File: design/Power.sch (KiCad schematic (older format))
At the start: 50 parts, among them U2 DRV8302, U3 NCP1117ST33T3G

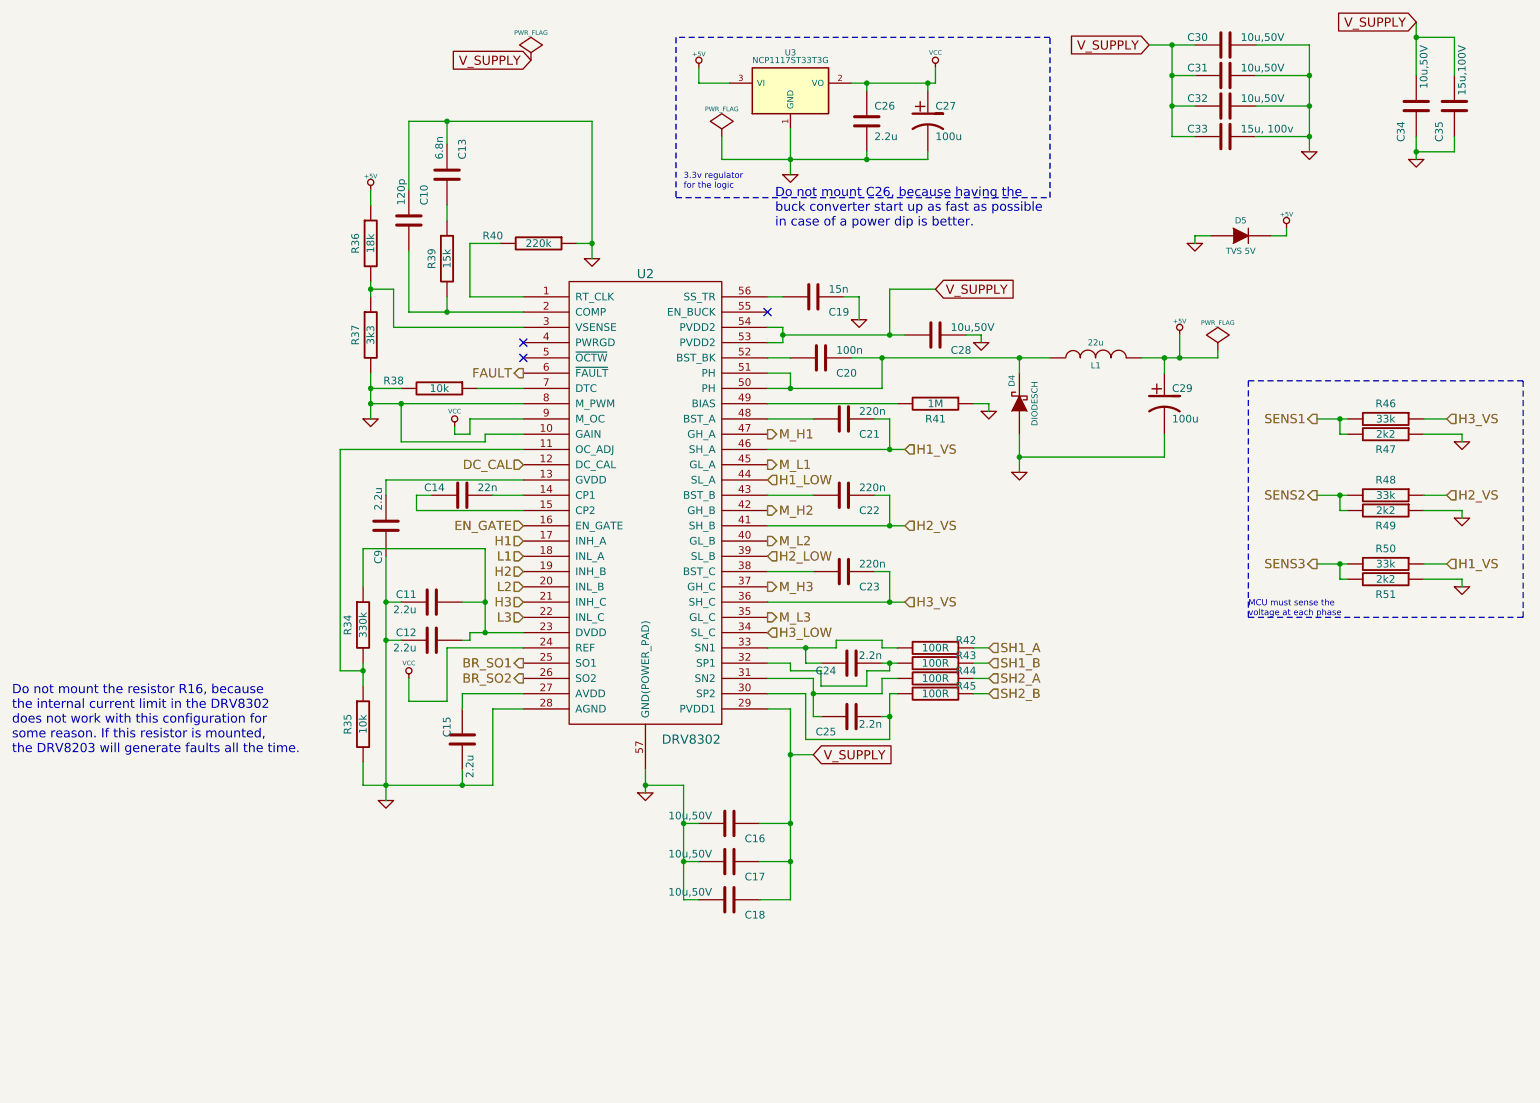
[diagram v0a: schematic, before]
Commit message: Add a voltage divider resistors for driver chip
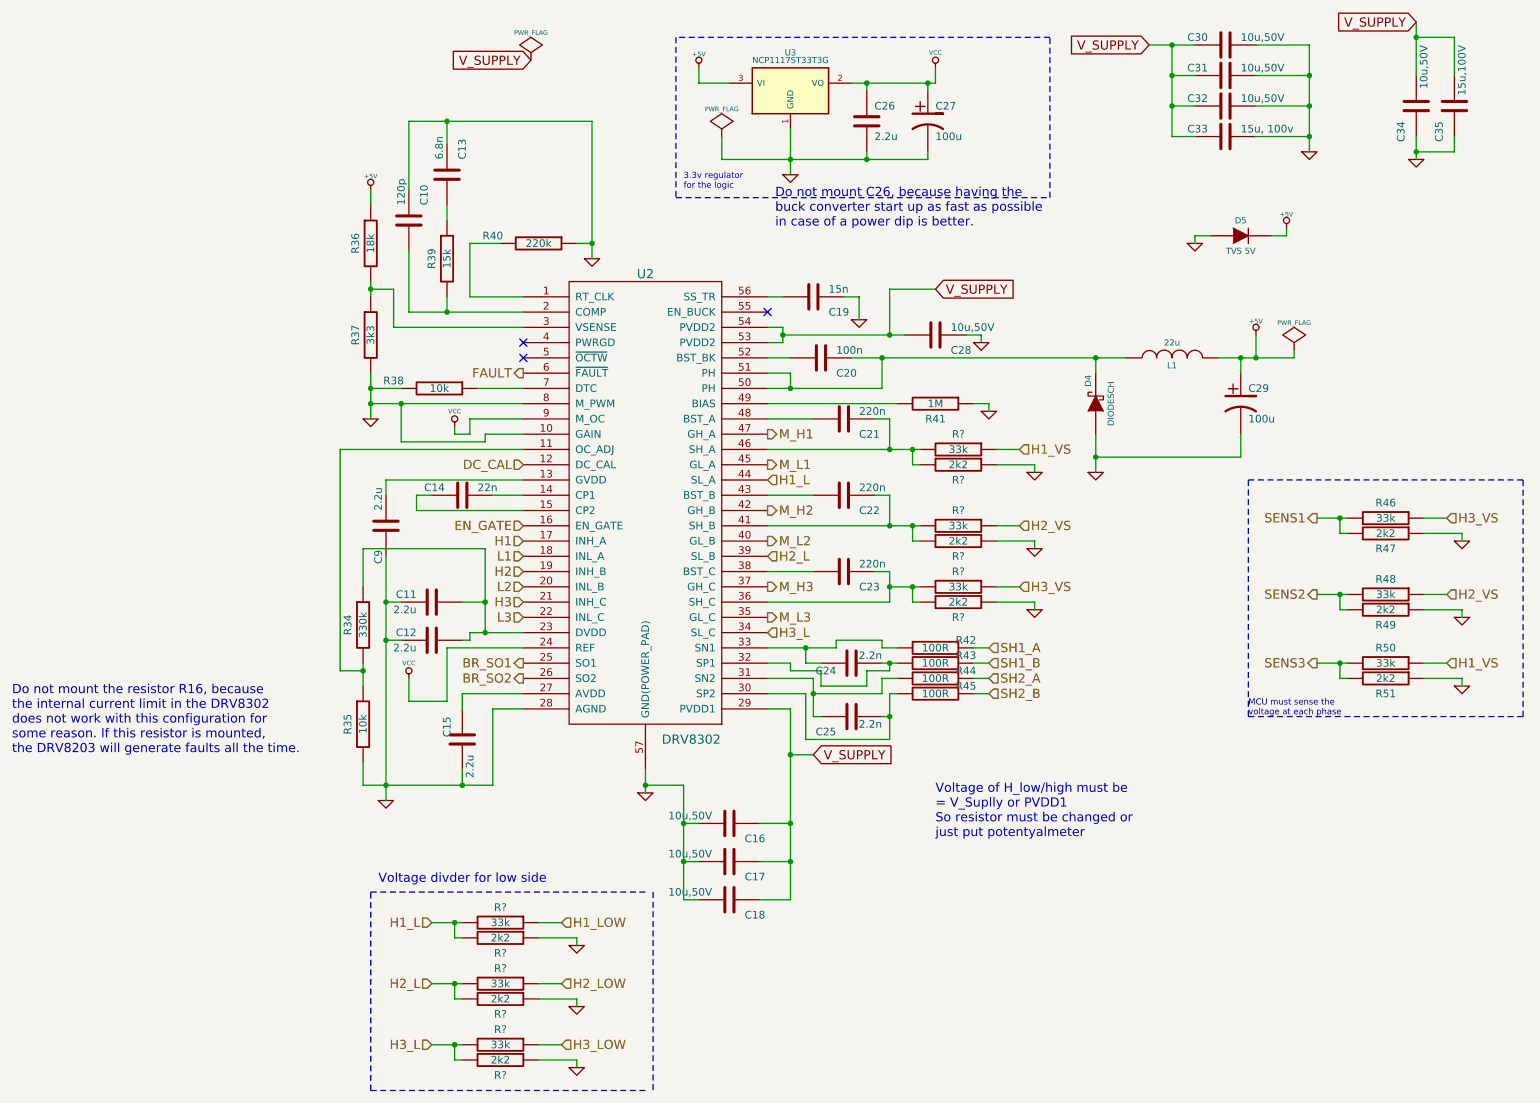
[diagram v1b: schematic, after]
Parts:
- added R? (x6): 33k, SMD_Packages:SMD-0603_r, symbol R
- added R? (x6): 2k2, SMD_Packages:SMD-0603_r, symbol R
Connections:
- net GND: now also R?.1, R?.1, R?.1, R?.1, R?.1, R?.1
- net H1_LOW: now also R?.1; no longer U2.44 (SL_A)
- net H1_VS: now also R?.1; no longer C21.1, U2.46 (SH_A)
- net H2_LOW: now also R?.1; no longer U2.39 (SL_B)
- net H2_VS: now also R?.1; no longer C22.1, U2.41 (SH_B)
- net H3_LOW: now also R?.1; no longer U2.34 (SL_C)
- net H3_VS: now also R?.1; no longer C23.1, U2.36 (SH_C)
- new net: C21.1, R?.2, R?.2, U2.46 (SH_A)
- new net: C23.1, R?.2, R?.2, U2.36 (SH_C)
- new net: C22.1, R?.2, R?.2, U2.41 (SH_B)
- new net H1_L: R?.2, R?.2, U2.44 (SL_A)
- new net H2_L: R?.2, R?.2, U2.39 (SL_B)
- new net H3_L: R?.2, R?.2, U2.34 (SL_C)
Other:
- note added: "Voltage divder for low side\n"
- note added: "Voltage of H_low/high must be \n= V_Suplly or PVDD1\nSo resistor must be changed or \njust put potentyalmeter"
- moved on the sheet: C29, D4, L1, R46, R47, R48, R49, R50, R51

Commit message: Declare mosfet supply
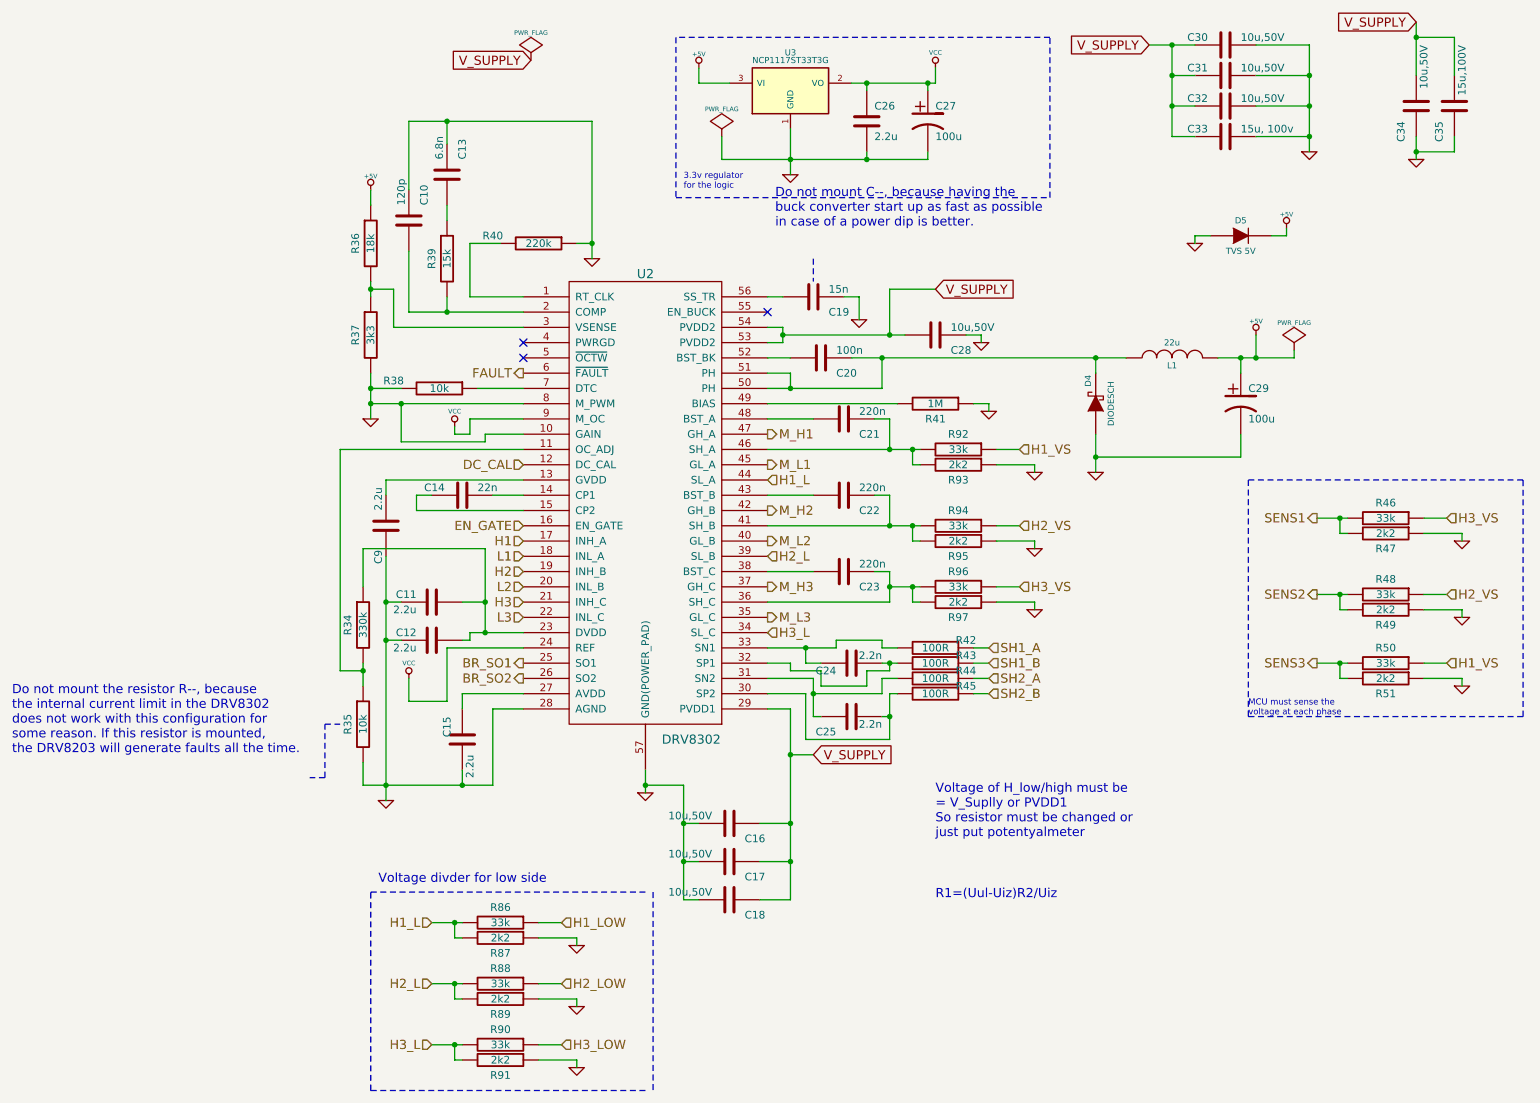
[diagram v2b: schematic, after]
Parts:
- gave numbers to parts that had none: 12
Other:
- note added: "Do not mount C--, because having the\nbuck converter start up as fast as possible\nin case of a power dip is better."
- note added: "Do not mount the resistor R--, because\nthe internal current limit in the DRV8302\ndoes not work with this configuration for\nsome reason. If this resistor is mounted, \nthe DRV8203 will generate faults all the time."
- note added: "R1=(Uul-Uiz)R2/Uiz"
- note removed: "Do not mount C26, because having the\nbuck converter start up as fast as possible\nin case of a power dip is better."
- note removed: "Do not mount the resistor R16, because\nthe internal current limit in the DRV8302\ndoes not work with this configuration for\nsome reason. If this resistor is mounted, \nthe DRV8203 will generate faults all the time."

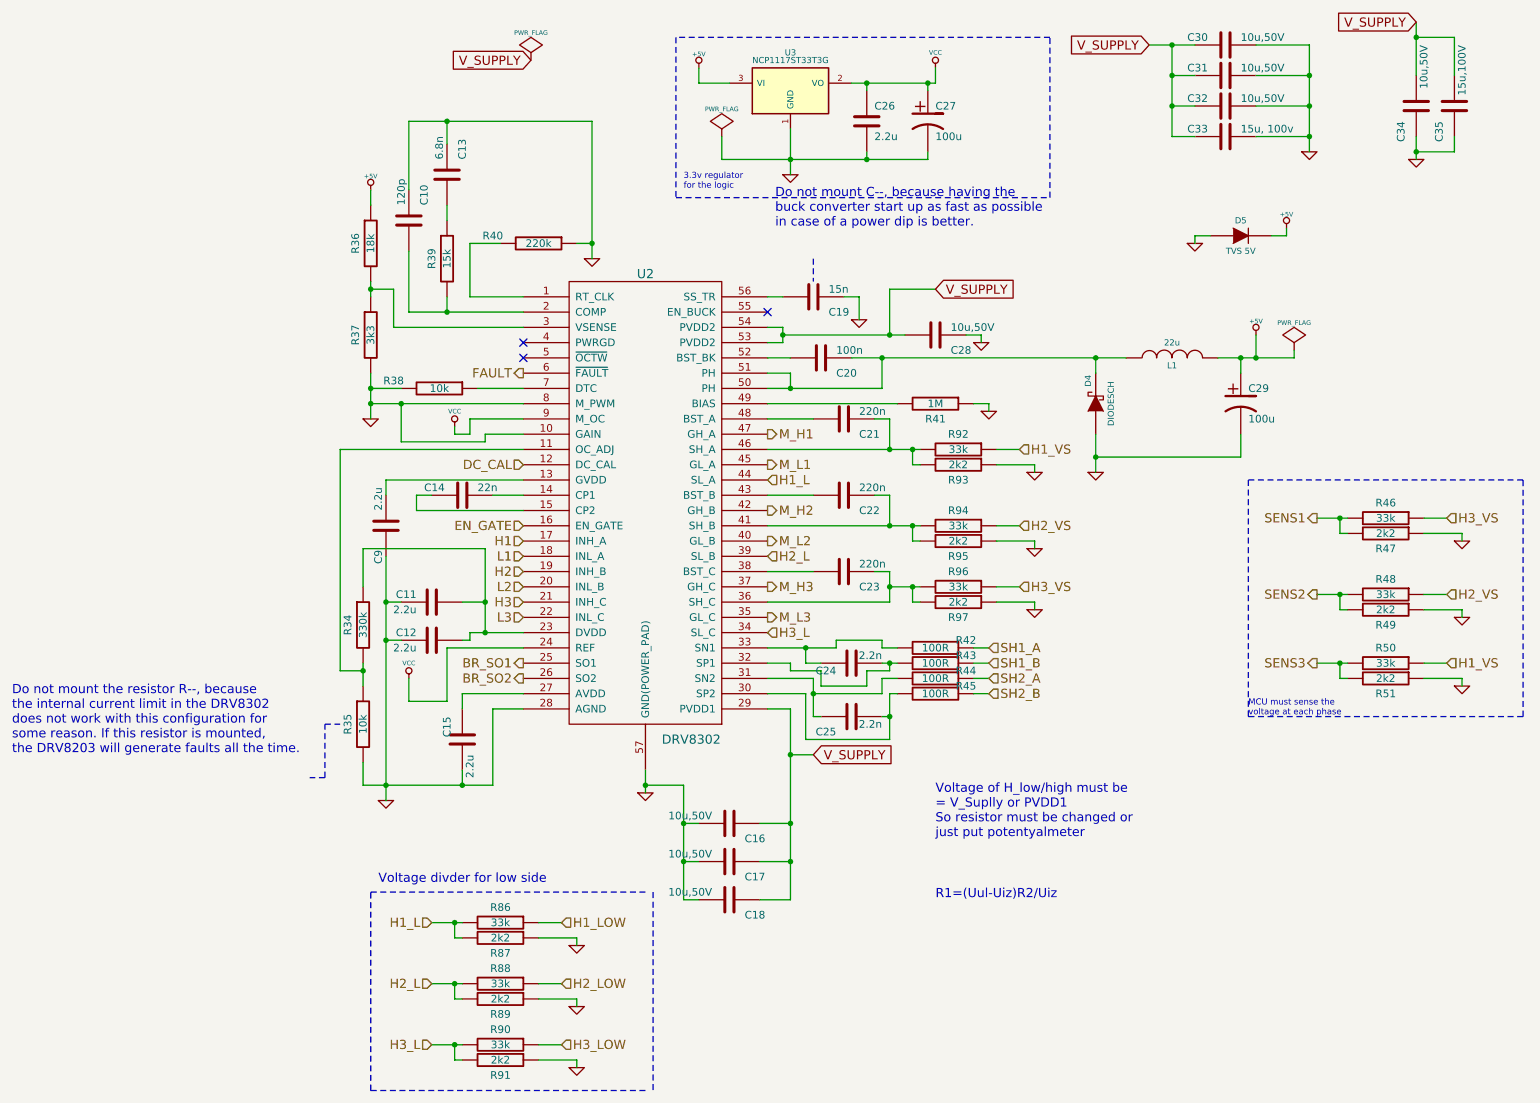
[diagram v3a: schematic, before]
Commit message: Add pwr for second motor
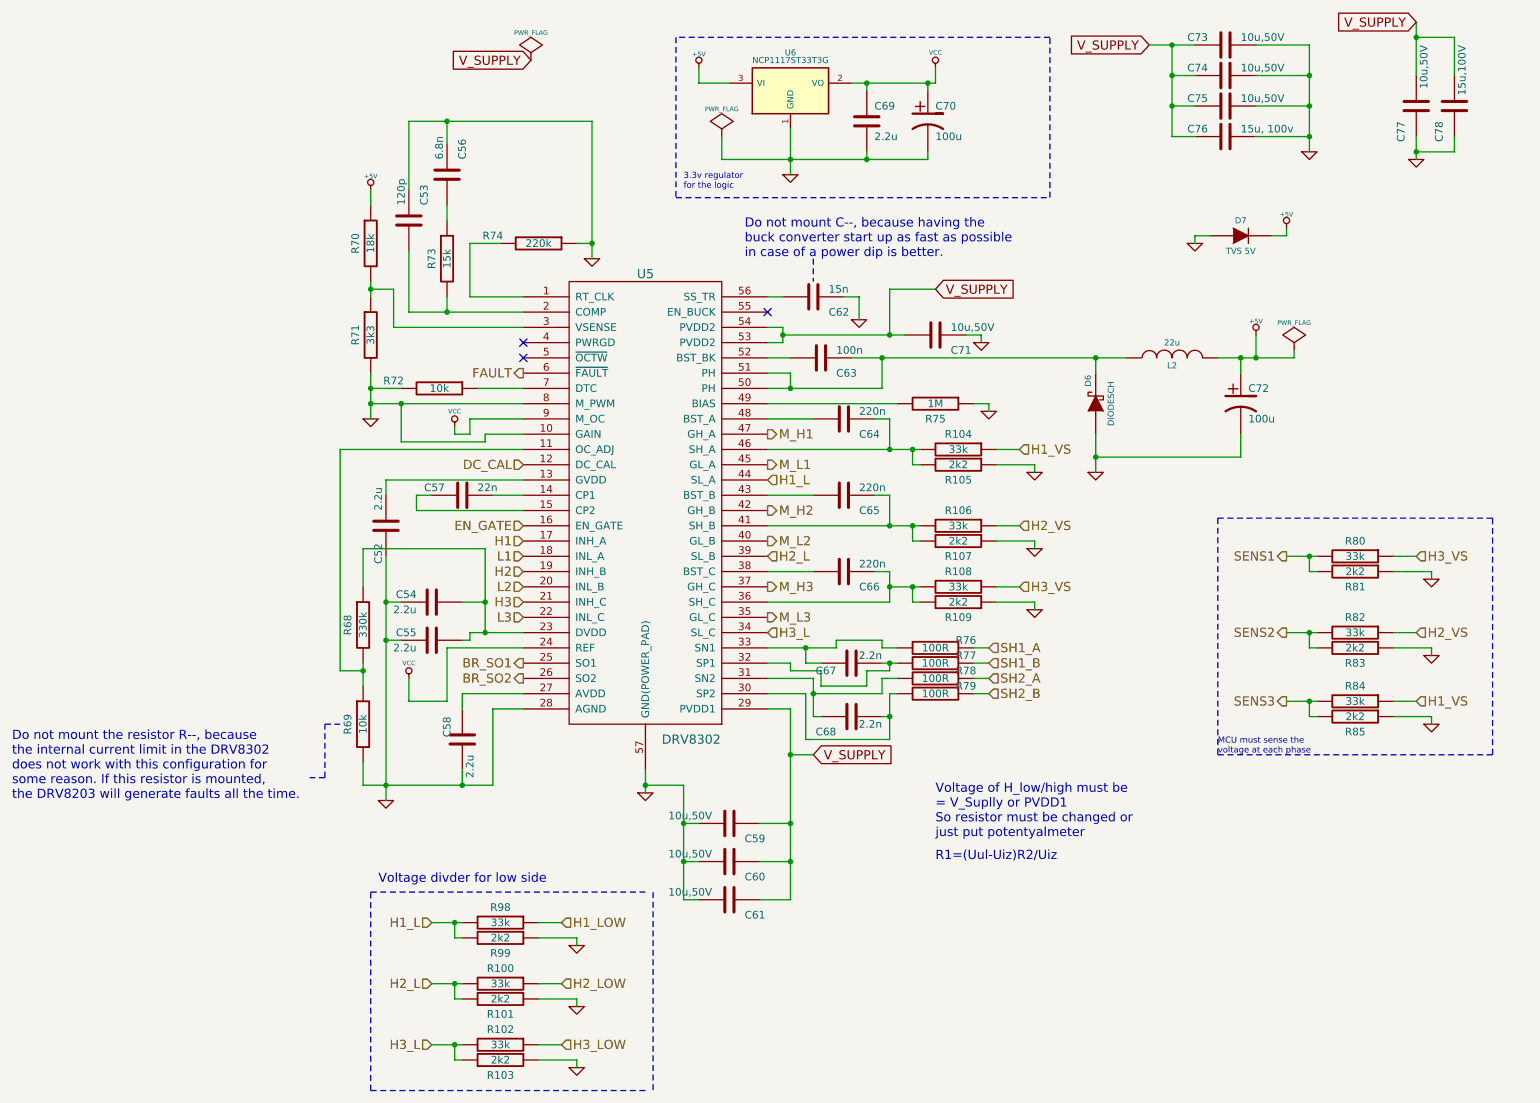
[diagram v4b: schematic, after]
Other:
- moved on the sheet: R80, R81, R82, R83, R84, R85
